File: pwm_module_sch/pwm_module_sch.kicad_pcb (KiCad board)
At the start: 2 copper layers, 53 parts, among them J1 SWIMM, J2 output -, J3 input, J4 output+, J5 uart, Q1 AO3400, Q2 IRFZ44N, SW1 ., SW2 ., U1 TM1637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

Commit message: transistor
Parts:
- C5, C6, D5, D6, D7, Q2, SW1, SW2: moved to B.Cu
- moved SW1 6.48 mm to (192.1, 87.3), turned to 180 degrees
- moved SW2 6.48 mm to (192.1, 94.9), turned to 180 degrees
- moved Q2 5.18 mm to (228.4, 91.2), turned to 0 degrees
- moved D6 5.10 mm to (196.6, 91.2), turned to 0 degrees
- moved D7 5.08 mm to (217.8, 91.2), turned to 0 degrees
- moved D5 5.08 mm to (207.2, 91.2), turned to 0 degrees
- moved R15 3.15 mm to (192.2, 53.4)
- moved R7 2.27 mm to (226.8, 83.2), turned to 90 degrees
- moved R16 2.19 mm to (189.3, 58.1), turned to 90 degrees
- moved R12 2.10 mm to (230.1, 86.7)
- moved C5 1.17 mm to (233.5, 86.7)
- moved J5 1.08 mm to (192.6, 55.6)
- moved D4 0.97 mm to (229.6, 81.9)
- moved R4 0.85 mm to (228.5, 93.0), turned to 180 degrees
- moved J4 0.76 mm to (231.8, 97.4)
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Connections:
- D7 pad 1: Net-(D6-Pad2) -> Net-(D5-Pad2)
- D7 pad 3: Net-(D5-Pad2) -> Net-(D6-Pad2)
- J5 pad 1: Net-(C14-Pad1) -> Net-(J5-Pad1)
- J5 pad 2: Net-(C13-Pad1) -> Net-(J5-Pad2)
- Q2 pad 2: +VSW -> +24V
- Q2 pad 3: +24V -> +VSW
- R15 pad 1: Net-(R15-Pad1) -> Net-(J5-Pad1)
- R16 pad 2: Net-(R16-Pad2) -> Net-(J5-Pad2)
- U2 pad 2: Net-(R15-Pad1) -> Net-(J5-Pad1)
- U2 pad 3: Net-(R16-Pad2) -> Net-(J5-Pad2)
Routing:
- net Net-(J5-Pad2): track 0.00 -> 8.79 mm
- net Net-(J5-Pad1): track 0.00 -> 6.09 mm
- net Net-(C13-Pad1): track 28.9 -> 23.7 mm
- net +24V: track 23.5 -> 28.2 mm
- net Net-(R16-Pad2): track 4.60 -> 0.00 mm
- net Net-(C14-Pad1): track 20.2 -> 17.2 mm
- net GND: track 324.2 -> 321.5 mm
- net +VSW: track 22.9 -> 20.3 mm
- net Net-(R15-Pad1): track 2.50 -> 0.00 mm
- net Net-(C3-Pad1): track 46.6 -> 45.9 mm
- net Net-(D4-Pad1): track 10.8 -> 10.2 mm

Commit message: inductor
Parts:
- added D9: ., Package_TO_SOT_THT:TO-220-3_Vertical, B.Cu at (229.2, 99.8)
- added L1: 100uH, Inductor_THT:L_Toroid_Vertical_L24.6mm_W15.5mm_P11.44mm_Pulse_KM-4, B.Cu at (224.3, 96.0)
- J5, R14: moved to B.Cu
- moved D3 35.0 mm to (218.5, 91.5), turned to 90 degrees
- moved J4 33.8 mm to (202.0, 81.6), turned to 180 degrees
- moved C5 24.9 mm to (209.0, 82.5)
- moved R12 24.0 mm to (206.7, 81.5), turned to 270 degrees
- moved C6 14.0 mm to (208.9, 96.5), turned to 90 degrees
- moved D5 13.0 mm to (197.4, 99.9)
- moved D6 13.0 mm to (186.8, 99.9)
- moved D7 13.0 mm to (208.0, 99.8)
- moved Q2 13.0 mm to (218.6, 99.8)
- moved R4 12.2 mm to (219.8, 101.7)
- moved J3 11.6 mm to (199.9, 105.5)
- moved R7 10.2 mm to (231.5, 92.3), turned to 0 degrees
- moved C10 9.43 mm to (220.7, 92.1), turned to 270 degrees
- moved C4 9.21 mm to (217.7, 87.4), turned to 90 degrees
- moved U3 8.94 mm to (225.0, 89.7)
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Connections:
- Q2 pad 3: +VSW -> Net-(D9-Pad2)
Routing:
- net GND: track 321.5 -> 378.7 mm
- net Net-(D9-Pad2): track 0.00 -> 16.6 mm
- net +VSW: track 20.3 -> 32.6 mm
- net Net-(D5-Pad2): track 26.9 -> 16.0 mm
- net +3V3: track 155.2 -> 165.9 mm
- net Net-(Q1-Pad3): track 40.6 -> 50.2 mm
- net Net-(C3-Pad1): track 45.9 -> 55.5 mm
- net Net-(SW1-Pad2): track 49.5 -> 43.4 mm
- net Net-(SW2-Pad2): track 56.1 -> 50.0 mm
- net Net-(C7-Pad1): track 17.0 -> 11.4 mm
- net Net-(C4-Pad1): track 38.1 -> 42.8 mm
- net Net-(D6-Pad2): track 51.4 -> 47.3 mm
- net Net-(C13-Pad1): track 23.7 -> 21.0 mm
- net -VSW: track 39.5 -> 37.4 mm
- net Net-(C1-Pad1): track 29.6 -> 27.7 mm
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
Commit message: board fixed
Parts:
- moved J4 32.4 mm to (233.8, 87.7)
- moved D5 31.8 mm to (229.2, 99.8)
- moved R12 31.7 mm to (235.7, 94.3), turned to 90 degrees
- moved C5 26.8 mm to (233.5, 93.3), turned to 270 degrees
- moved D7 21.2 mm to (186.8, 99.8)
- moved D9 21.2 mm to (208.0, 99.8)
- moved D6 10.6 mm to (197.4, 99.8)
- moved L1 6.72 mm to (218.0, 93.8)
- moved C6 6.09 mm to (203.3, 94.3), turned to 180 degrees
- moved R7 4.48 mm to (227.8, 89.8)
- moved D4 4.46 mm to (227.8, 87.0)
- moved U3 4.42 mm to (221.3, 87.2)
- moved C10 4.42 mm to (217.1, 89.6)
- moved C3 4.42 mm to (225.5, 86.0)
- moved C4 4.42 mm to (214.0, 85.0)
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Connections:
- D7 pad 1: Net-(D5-Pad2) -> GND
- D7 pad 2: +24V -> Net-(D7-Pad2)
- D7 pad 3: Net-(D6-Pad2) -> GND
- D9 pad 1: GND -> Net-(D6-Pad2)
- D9 pad 2: Net-(D9-Pad2) -> +24V
- D9 pad 3: GND -> Net-(D7-Pad2)
- J3 pad 1: Net-(D5-Pad2) -> Net-(D6-Pad2)
- J3 pad 2: Net-(D6-Pad2) -> Net-(D7-Pad2)
- L1 pad 1: Net-(D9-Pad2) -> Net-(D5-Pad2)
- Q2 pad 3: Net-(D9-Pad2) -> Net-(D5-Pad2)
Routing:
- net Net-(D7-Pad2): track 0.00 -> 45.2 mm
- net GND: track 378.7 -> 422.9 mm
- net Net-(D6-Pad2): track 47.3 -> 16.0 mm
- net Net-(D9-Pad2): track 16.6 -> 0.00 mm
- net Net-(D5-Pad2): track 16.0 -> 23.6 mm
- net +24V: track 28.9 -> 35.4 mm
- net Net-(C3-Pad1): track 55.5 -> 50.0 mm
- net +3V3: track 165.9 -> 161.0 mm
- net -VSW: track 37.4 -> 32.7 mm
- net Net-(C4-Pad1): track 42.8 -> 38.1 mm
- net Net-(D4-Pad1): track 10.1 -> 8.49 mm

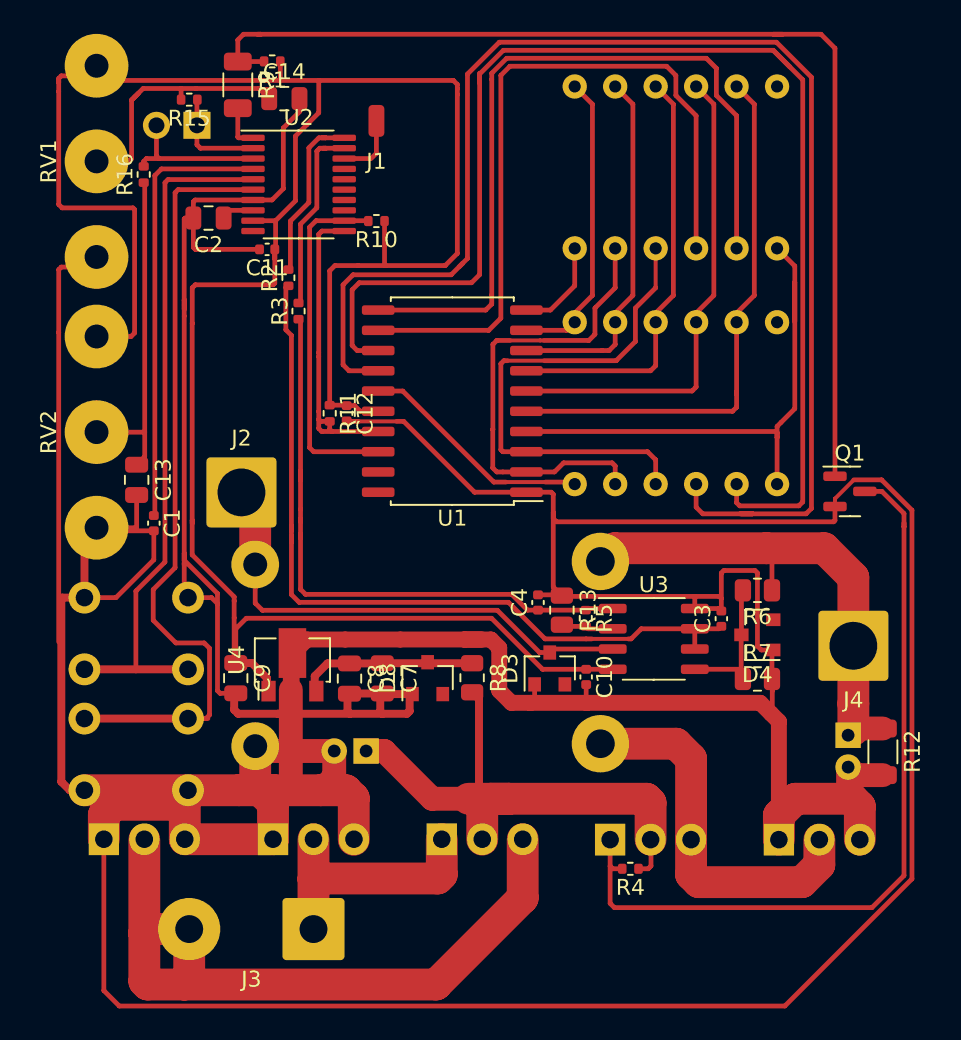
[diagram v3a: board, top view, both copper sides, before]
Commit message: mosfet driver added
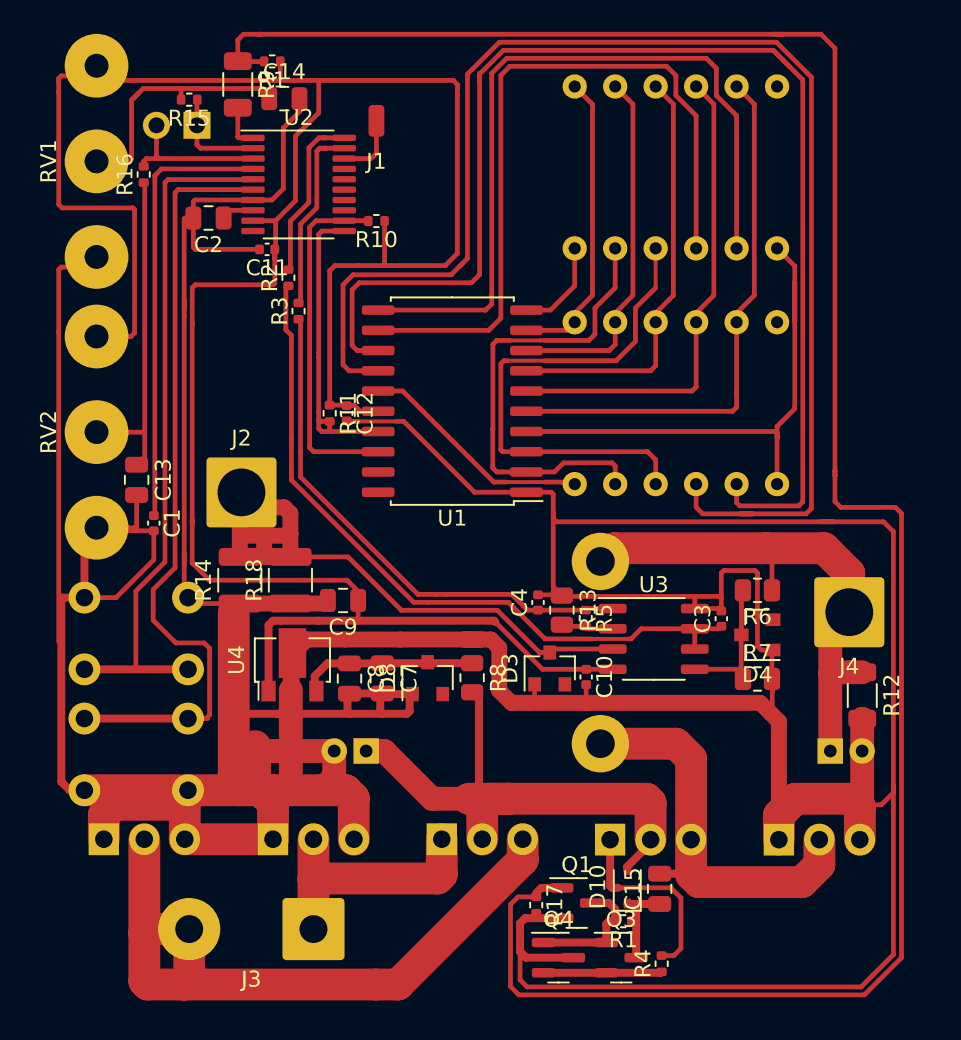
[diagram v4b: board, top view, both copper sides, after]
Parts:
- added C15: 10uF, Capacitor_SMD:C_0805_2012Metric, F.Cu at (221.7, 102.9)
- added D10: 1N5822, Diode_SMD:D_SOD-323, F.Cu at (219.6, 102.8)
- added Q3: MMBTA42, Package_TO_SOT_SMD:SOT-23, F.Cu at (219.3, 107.3)
- added Q4: MMBTA92, Package_TO_SOT_SMD:SOT-23, F.Cu at (215.3, 107.3)
- added R1: 100k, Resistor_SMD:R_0402_1005Metric, F.Cu at (219.4, 105.0)
- added R17: 1k, Resistor_SMD:R_0402_1005Metric, F.Cu at (213.9, 104.0)
- added R18: 0.01R, Resistor_SMD:R_1210_3225Metric, F.Cu at (198.5, 83.6)
- R14: footprint Resistor_THT:R_Bare_Metal_Element_L12.4mm_W4.8mm_P11.40mm -> Resistor_SMD:R_1210_3225Metric; moved to F.Cu
- R4: value 100k -> 1k
- moved Q1 31.0 mm to (216.5, 103.8)
- moved R14 10.5 mm to (195.3, 83.6)
- moved C9 8.31 mm to (201.8, 84.8), turned to 180 degrees
- moved R4 6.27 mm to (221.8, 107.6), turned to 90 degrees
- moved R12 3.76 mm to (234.4, 90.8)
- moved J4 2.12 mm to (233.6, 85.6)
- moved C5 1.49 mm to (232.4, 94.3), turned to 0 degrees
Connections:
- D3 pad 1: -VSW -> GND
- D3 pad 2: GND -> unconnected-(D3-Pad2)
- D4 pad 1: Net-(D4-Pad1) -> GND
- D4 pad 2: GND -> unconnected-(D4-Pad2)
- D8 pad 1: Net-(C7-Pad1) -> GND
- D8 pad 2: GND -> unconnected-(D8-Pad2)
- J4 pad 1: +VSW -> unconnected-(J4-Pad1)
- Q1 pad 3: Net-(Q1-Pad3) -> Net-(Q3-Pad1)
- Q2 pad 1: Net-(Q1-Pad3) -> Net-(Q2-Pad1)
- R4 pad 1: +24V -> Net-(Q3-Pad2)
- R4 pad 2: Net-(Q1-Pad3) -> Net-(Q2-Pad1)
- R6 pad 2: Net-(D4-Pad1) -> Net-(D4-Pad3)
- R7 pad 1: Net-(D4-Pad1) -> Net-(D4-Pad3)
- U1 pad 19: Net-(U1-Pad19) -> unconnected-(U1-Pad19)
- U1 pad 20: Net-(U1-Pad20) -> unconnected-(U1-Pad20)
- U2 pad 10: Net-(U2-Pad10) -> unconnected-(U2-Pad10)
- U2 pad 13: Net-(U2-Pad13) -> unconnected-(U2-Pad13)
- U2 pad 14: Net-(U2-Pad14) -> unconnected-(U2-Pad14)
- U2 pad 15: Net-(U2-Pad15) -> unconnected-(U2-Pad15)
- U2 pad 16: Net-(U2-Pad16) -> unconnected-(U2-Pad16)
- U2 pad 17: Net-(U2-Pad17) -> unconnected-(U2-Pad17)
- U3 pad 5: Net-(D4-Pad1) -> Net-(D4-Pad3)
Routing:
- net Net-(Q1-Pad1): track 68.9 -> 137.6 mm
- net Net-(Q1-Pad3): track 50.2 -> 0.00 mm
- net GND: track 422.9 -> 409.2 mm
- net Net-(Q2-Pad1): track 0.00 -> 12.2 mm
- net -VSW: track 32.7 -> 42.4 mm
- net Net-(D4-Pad3): track 0.00 -> 8.49 mm
- net Net-(D4-Pad1): track 8.49 -> 0.00 mm
- net Net-(Q3-Pad1): track 0.00 -> 8.12 mm
- net Net-(Q3-Pad2): track 0.00 -> 7.44 mm
- net Net-(C15-Pad1): track 0.00 -> 5.79 mm
- net Net-(C4-Pad1): track 38.1 -> 33.1 mm
- net Net-(C3-Pad1): track 50.0 -> 45.1 mm
- net +3V3: track 161.0 -> 163.1 mm
- net Net-(Q2-Pad3): track 23.6 -> 25.1 mm
- net Net-(D7-Pad2): track 45.2 -> 43.8 mm
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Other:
- net class Default removed
